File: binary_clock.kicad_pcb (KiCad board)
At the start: 2 copper layers, 120 x 50 mm, 87 parts, among them J1 Conn_01x03_Pin, P1 TYPE-C-31-M-12, SW1 TS-1088-AR02016, SW2 TS-1088-AR02016, SW3 TS-1088-AR02016, SW4 TS-1088-AR02016, SW5 TIMEZONE_CHANGE, U1 RP2040, U2 W25Q32JVSS, U3 AMS1117-3.3, U4 DS3231M, U5 AT24C32_SOIC, Y1 ABM8-272-T3

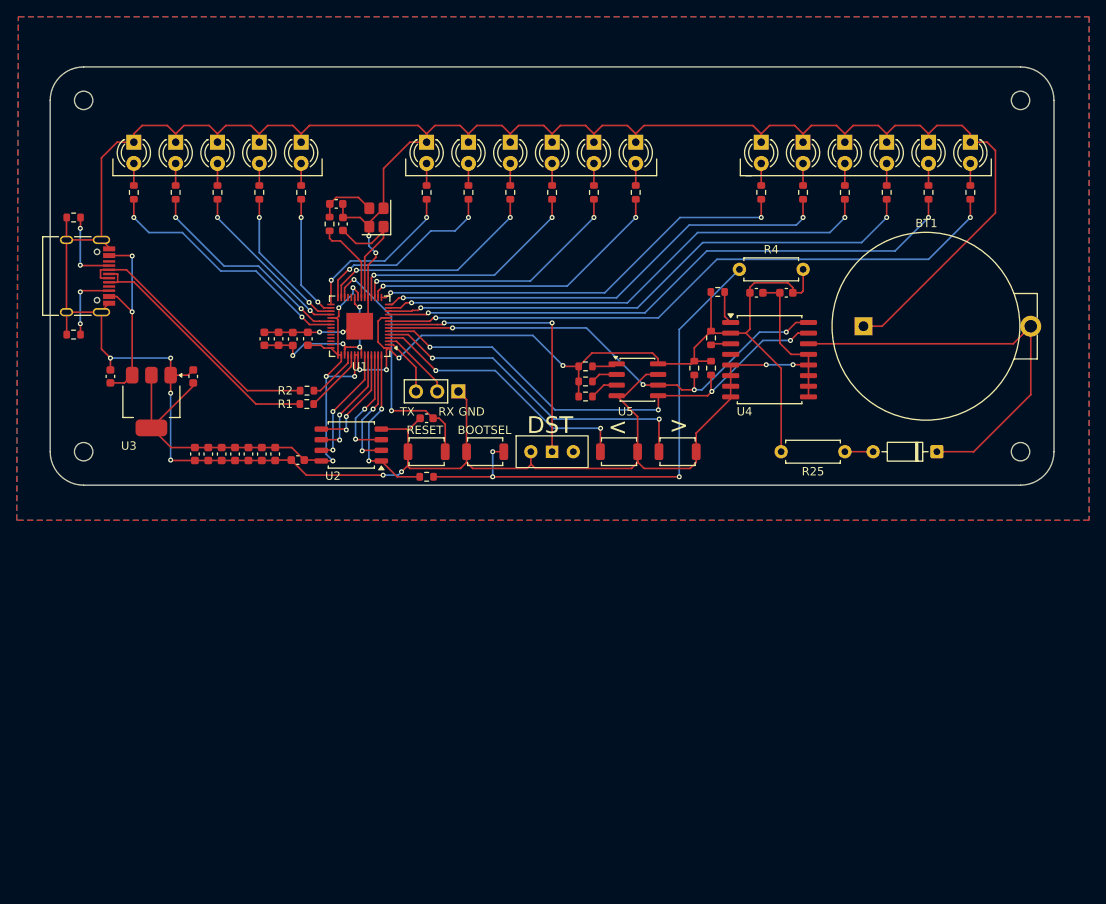
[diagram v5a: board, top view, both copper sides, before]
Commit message: Widen power tracks and improve solderability
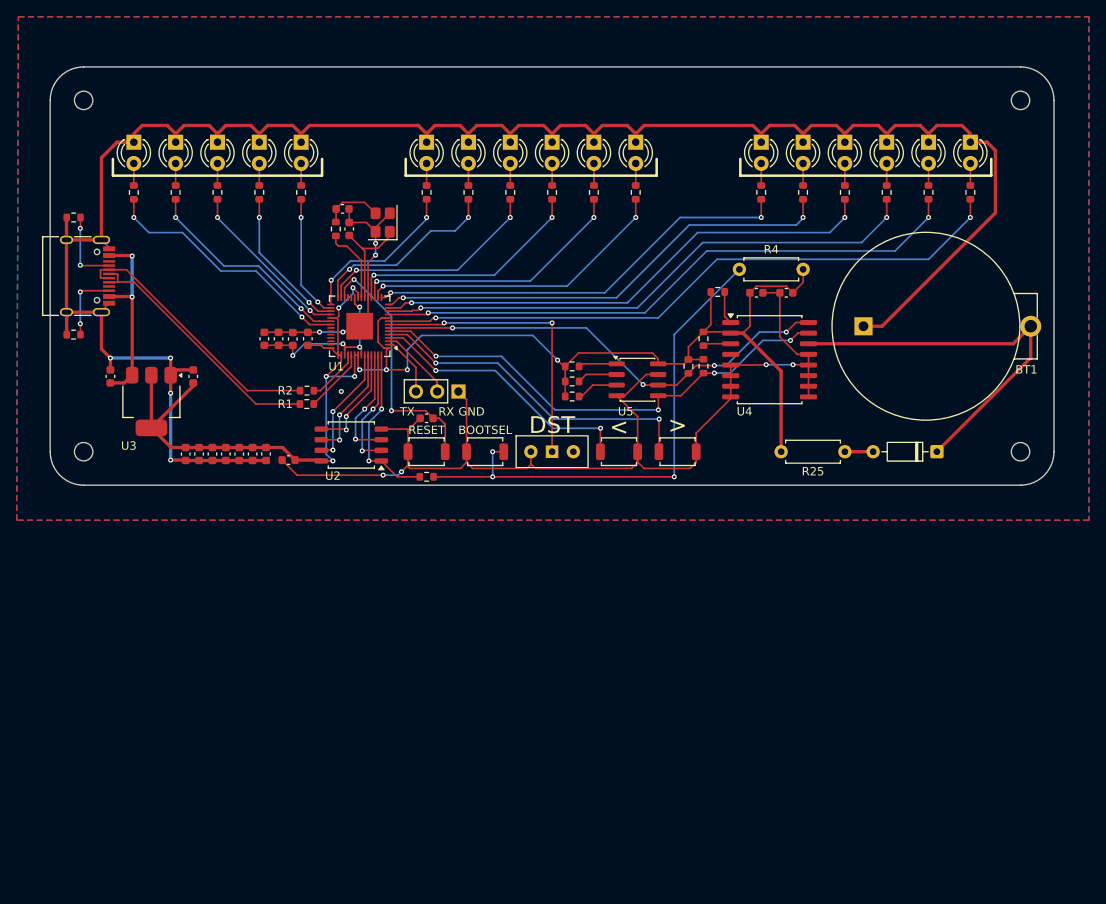
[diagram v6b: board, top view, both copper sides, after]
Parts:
- BT1: value CR2032 -> CR2032_holder
- moved R30 1.60 mm to (166.4, 101.8)
- moved R31 1.60 mm to (166.4, 103.6)
- moved R32 1.60 mm to (166.4, 105.4)
- moved C10 1.10 mm to (128.2, 112.3)
- moved C6 1.10 mm to (121.8, 112.3)
- moved C9 1.10 mm to (126.6, 112.3)
- moved C11 1.10 mm to (129.8, 112.3)
- moved C13 1.10 mm to (132.5, 113.0)
- moved C5 1.10 mm to (120.2, 112.3)
- moved C7 1.10 mm to (123.4, 112.3)
- moved C8 1.10 mm to (125.0, 112.3)
- moved C14 0.96 mm to (139.8, 85.4)
- moved C15 0.96 mm to (138.9, 83.0)
- moved R5 0.96 mm to (138.2, 85.4)
- moved Y1 0.96 mm to (143.8, 84.6)
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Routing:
- net GND: track 420.4 -> 406.0 mm, vias 12 -> 13
- net /XIN: track 16.0 -> 12.6 mm
- net Net-(BT1-+): track 49.7 -> 47.1 mm
- net /SCL: track 58.4 -> 56.1 mm
- net /SDA: track 61.0 -> 58.9 mm
- net Net-(U5-A0): track 3.03 -> 4.63 mm
- net Net-(U5-A1): track 3.25 -> 4.85 mm
- net Net-(U5-A2): track 3.47 -> 5.07 mm
- net Net-(U4-~{INT}/SQW): track 2.40 -> 3.35 mm
- net /XOUT: track 10.1 -> 9.21 mm
- net Net-(U3-VI): track 23.5 -> 22.8 mm

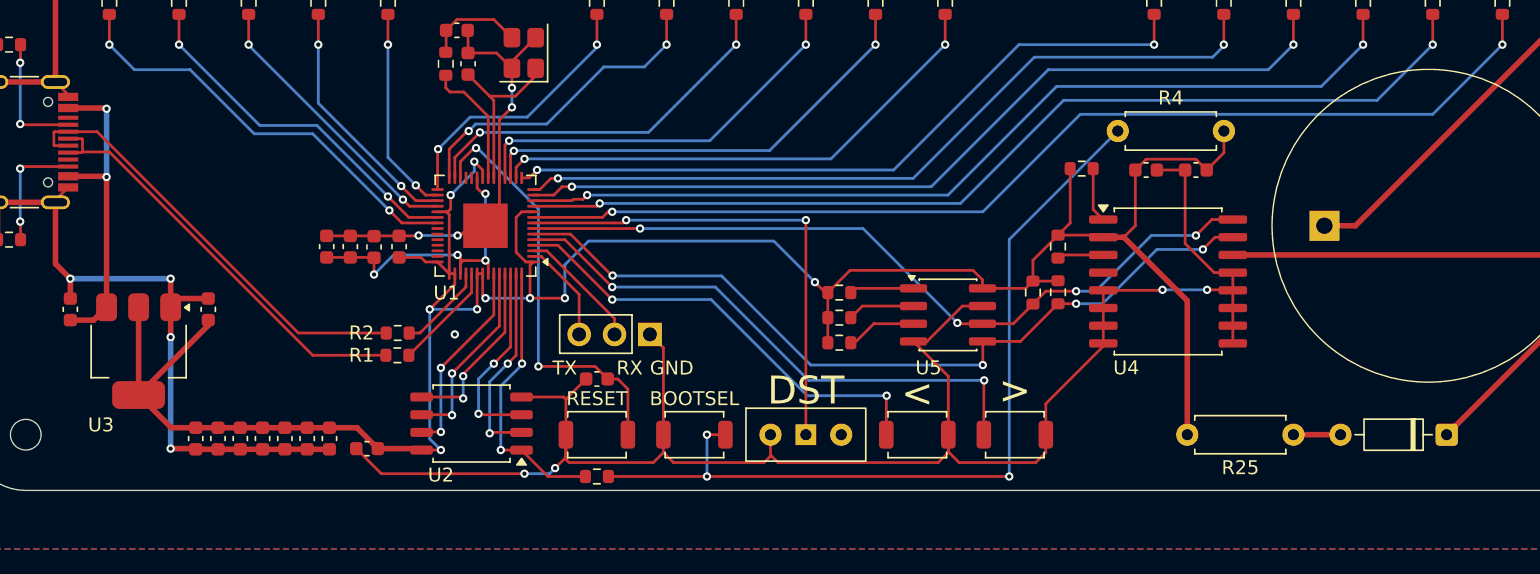
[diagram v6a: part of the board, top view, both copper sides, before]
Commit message: change silkscreen, adjust footprints
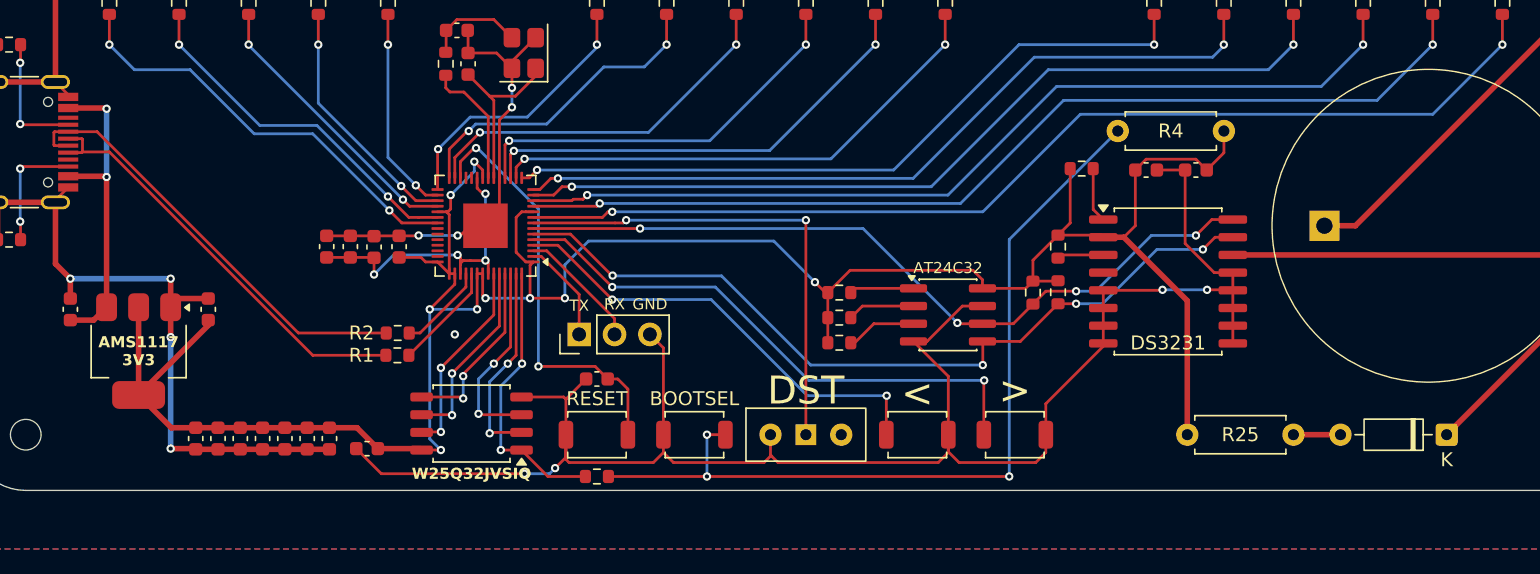
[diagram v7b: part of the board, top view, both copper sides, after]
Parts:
- renumbered 0 to MH1, 0 to MH2, 0 to MH3, 0 to MH4
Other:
- board text added: "AMS1117 3V3"
- board text added: "AT24C32"
- board text added: "DS3231"
- board text added: "W25Q32JVSIQ"

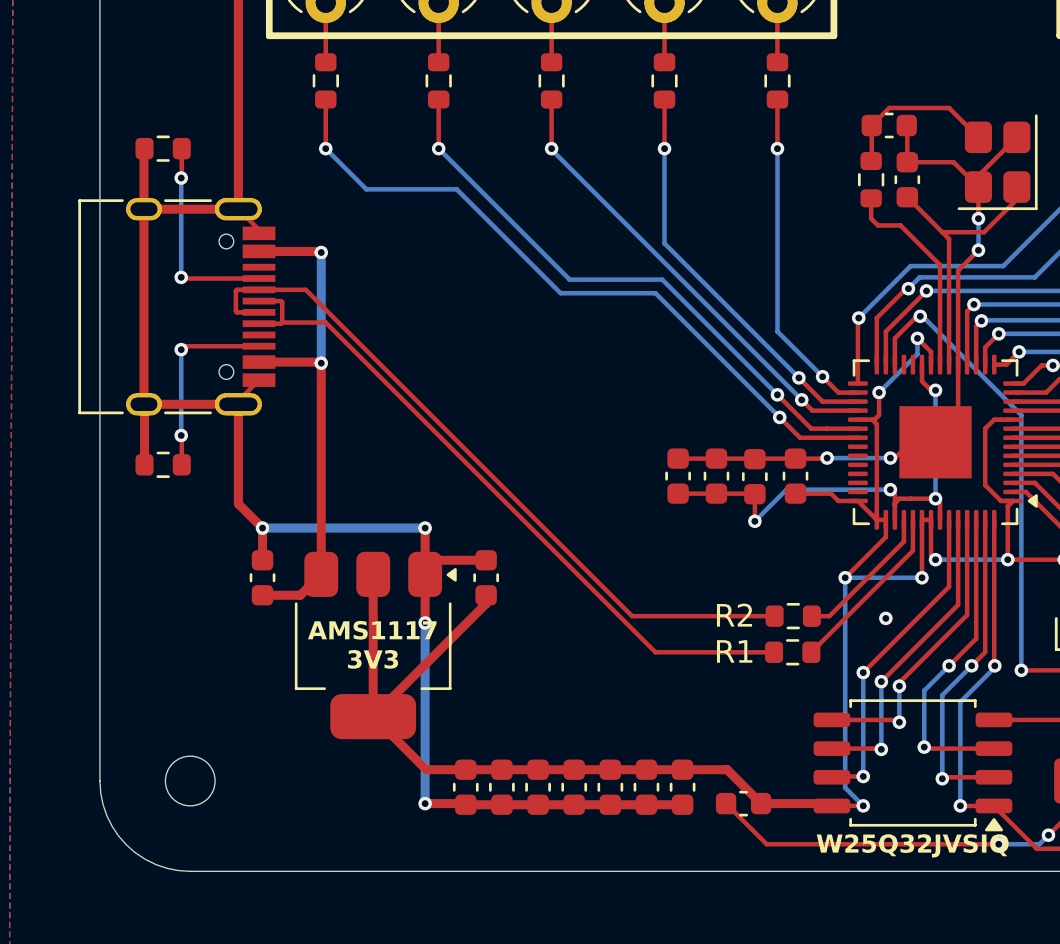
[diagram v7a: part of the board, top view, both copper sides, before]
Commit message: update USB differential pair geometry for 90 ohm coplanar impedance
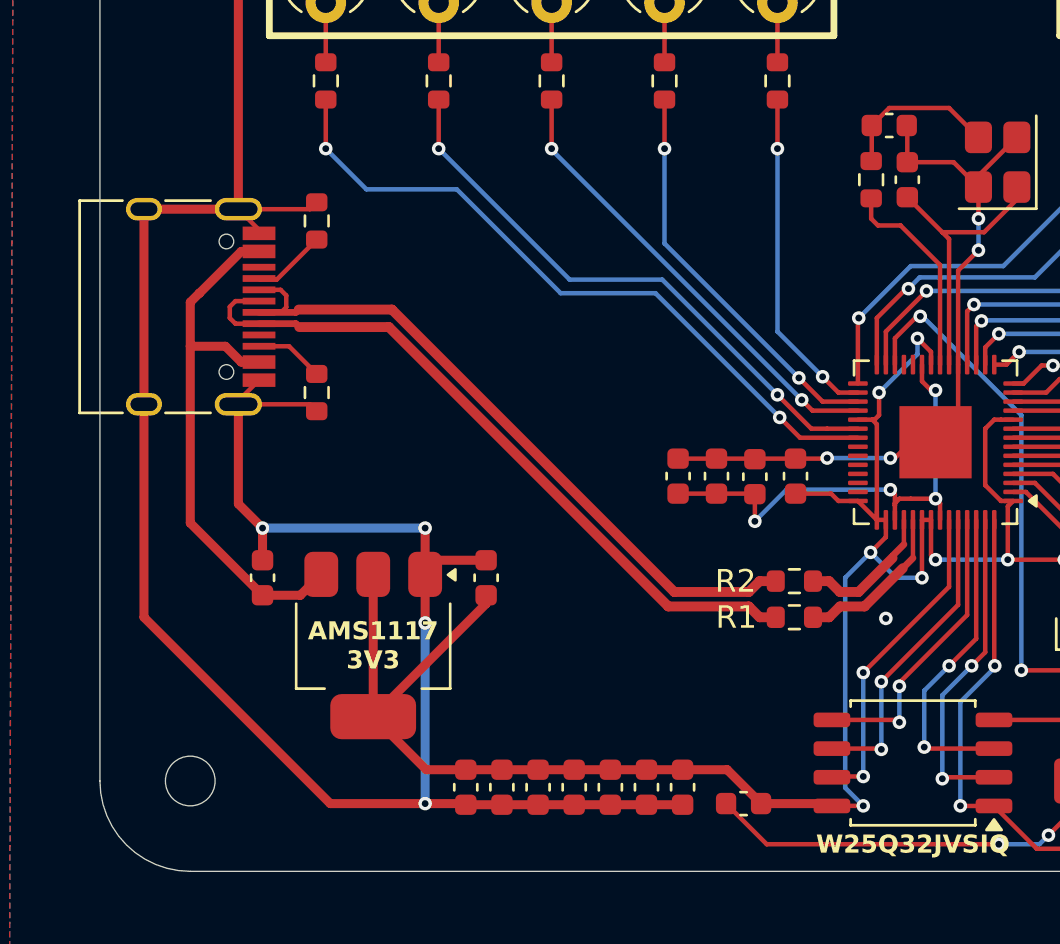
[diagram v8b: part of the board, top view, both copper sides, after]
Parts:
- moved R6 7.52 mm to (113.6, 87.2), turned to 90 degrees
- moved R7 7.52 mm to (113.6, 94.8), turned to -90 degrees
- moved R1 1.55 mm to (134.8, 104.8)
- moved R2 1.55 mm to (134.8, 103.2)
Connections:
- net /USB_DM renamed /USB_N
- net /USB_DP renamed /USB_P
- net Net-(U1-USB_DM) renamed /RP_USB_N
- net Net-(U1-USB_DP) renamed /RP_USB_P
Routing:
- net GND: track 406.0 -> 429.2 mm
- net Net-(P1-CC1): track 9.18 -> 3.31 mm, vias 2 -> 0
- net Net-(P1-CC2): track 8.62 -> 3.06 mm, vias 2 -> 0
- net Net-(U3-VI): track 22.8 -> 24.6 mm, vias 2 -> 0
- net /USB_P: track 30.8 -> 31.6 mm
- net +3.3V: track 178.4 -> 177.8 mm
- net /RP_USB_P: track 7.73 -> 7.20 mm
